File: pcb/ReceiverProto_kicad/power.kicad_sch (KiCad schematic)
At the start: 8 parts, among them U11 ADM8660ARZ-REEL, U12 ADP7182AUJZ-1.8-R7

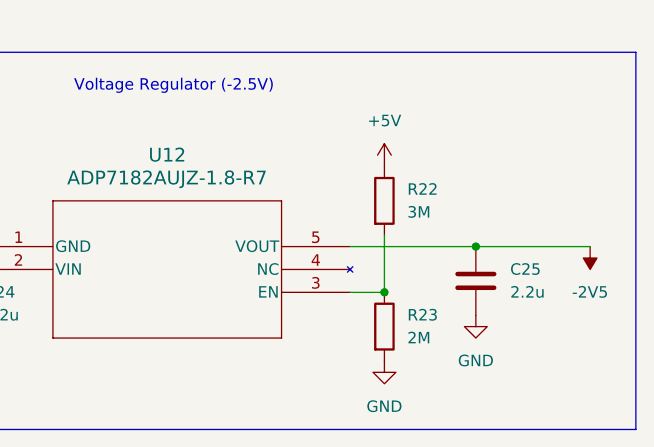
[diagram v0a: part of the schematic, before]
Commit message: added I/O for ADC interface, other slight tweaks
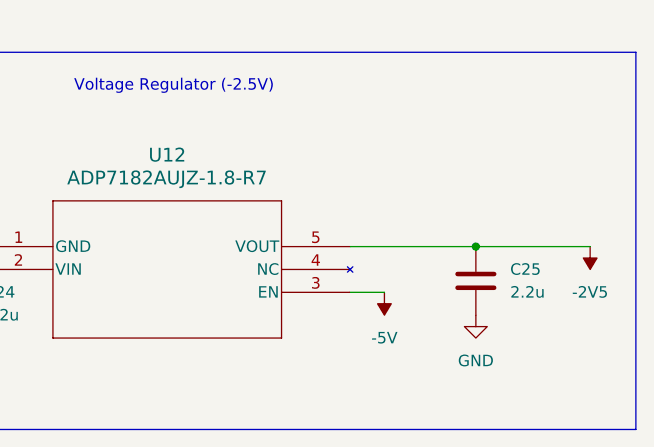
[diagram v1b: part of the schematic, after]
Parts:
- removed R22: 3M, symbol Device:R
- removed R23: 2M, symbol Device:R
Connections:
- net -5V: now also U12.3 (EN)
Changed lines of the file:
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@@
 		(color 0 0 0 0)
 	)
-	(junction
-		(at 234.95 72.39)
-		(diameter 0)
-		(color 0 0 0 0)
-	)
 	(wire
 		(pts
@@
 		(pts
 			(xy 231.14 72.39) (xy 234.95 72.39)
-		)
-		(stroke
-			(width 0)
-			(type default)
-		)
-	)
-	(wire
-		(pts
-			(xy 234.95 66.04) (xy 234.95 72.39)
 		)
 		(stroke
@@
 	)
 	(symbol
-		(lib_id "Device:R")
-		(at 234.95 62.23 0)
-		(unit 1)
-		(exclude_from_sim no)
-		(in_bom yes)
-		(on_board yes)
-		(dnp no)
-		(fields_autoplaced yes)
-		(property "Reference" "R22"
-			(at 237.49 60.9599 0)
-			(effects
-				(font
-					(size 1.27 1.27)
-				)
-				(justify left)
-			)
-		)
-		(property "Value" "3M"
-			(at 237.49 63.4999 0)
-			(effects
-				(font
-					(size 1.27 1.27)
-				)
-				(justify left)
-			)
-		)
-		(property "Footprint" ""
-			(at 233.172 62.23 90)
-			(effects
-				(font
-					(size 1.27 1.27)
-				)
-				(hide yes)
-			)
-		)
-		(property "Datasheet" "~"
-			(at 234.95 62.23 0)
-			(effects
-				(font
-					(size 1.27 1.27)
-				)
-				(hide yes)
-			)
-		)
-		(property "Description" "Resistor"
-			(at 234.95 62.23 0)
-			(effects
-				(font
-					(size 1.27 1.27)
-				)
-				(hide yes)
-			)
-		)
-		(pin "1"
-		)
-		(pin "2"
-		)
-		(instances
-			(project ""
-				(path "/1f346c8c-1e51-4f75-85ee-2d30c45e3fc5/93d8b42a-fb95-4bca-8da9-6ca00464e9a7"
-					(reference "R22")
-					(unit 1)
-				)
-			)
-		)
-	)
-	(symbol
 		(lib_id "power:-2V5")
 		(at 257.81 67.31 180)
@@
 	)
 	(symbol
-		(lib_id "Device:R")
-		(at 234.95 76.2 0)
-		(unit 1)
-		(exclude_from_sim no)
-		(in_bom yes)
-		(on_board yes)
-		(dnp no)
-		(fields_autoplaced yes)
-		(property "Reference" "R23"
-			(at 237.49 74.9299 0)
-			(effects
-				(font
-					(size 1.27 1.27)
-				)
-				(justify left)
-			)
-		)
-		(property "Value" "2M"
-			(at 237.49 77.4699 0)
-			(effects
-				(font
-					(size 1.27 1.27)
-				)
-				(justify left)
-			)
-		)
-		(property "Footprint" ""
-			(at 233.172 76.2 90)
-			(effects
-				(font
-					(size 1.27 1.27)
-				)
-				(hide yes)
-			)
-		)
-		(property "Datasheet" "~"
-			(at 234.95 76.2 0)
-			(effects
-				(font
-					(size 1.27 1.27)
-				)
-				(hide yes)
-			)
-		)
-		(property "Description" "Resistor"
-			(at 234.95 76.2 0)
-			(effects
-				(font
-					(size 1.27 1.27)
-				)
-				(hide yes)
-			)
-		)
-		(pin "1"
-		)
-		(pin "2"
-		)
-		(instances
-			(project ""
-				(path "/1f346c8c-1e51-4f75-85ee-2d30c45e3fc5/93d8b42a-fb95-4bca-8da9-6ca00464e9a7"
-					(reference "R23")
-					(unit 1)
-				)
-			)
-		)
-	)
-	(symbol
 		(lib_id "power:GND")
 		(at 186.69 77.47 0)
@@
 	)
 	(symbol
-		(lib_id "power:+5V")
-		(at 234.95 58.42 0)
-		(unit 1)
-		(exclude_from_sim no)
-		(in_bom yes)
-		(on_board yes)
-		(dnp no)
-		(fields_autoplaced yes)
-		(property "Reference" "#PWR057"
-			(at 234.95 62.23 0)
-			(effects
-				(font
-					(size 1.27 1.27)
-				)
-				(hide yes)
-			)
-		)
-		(property "Value" "+5V"
-			(at 234.95 53.34 0)
-			(effects
-				(font
-					(size 1.27 1.27)
-				)
-			)
-		)
-		(property "Footprint" ""
-			(at 234.95 58.42 0)
-			(effects
-				(font
-					(size 1.27 1.27)
-				)
-				(hide yes)
-			)
-		)
-		(property "Datasheet" ""
-			(at 234.95 58.42 0)
-			(effects
-				(font
-					(size 1.27 1.27)
-				)
-				(hide yes)
-			)
-		)
-		(property "Description" "Power symbol creates a global label with name \"+5V\""
-			(at 234.95 58.42 0)
-			(effects
-				(font
-					(size 1.27 1.27)
-				)
-				(hide yes)
-			)
-		)
-		(pin "1"
-		)
-		(instances
-			(project ""
-				(path "/1f346c8c-1e51-4f75-85ee-2d30c45e3fc5/93d8b42a-fb95-4bca-8da9-6ca00464e9a7"
-					(reference "#PWR057")
-					(unit 1)
-				)
-			)
-		)
-	)
-	(symbol
 		(lib_id "Device:C")
 		(at 186.69 73.66 0)
@@
 	)
 	(symbol
+		(lib_id "power:-5V")
+		(at 234.95 72.39 180)
+		(unit 1)
+		(exclude_from_sim no)
+		(in_bom yes)
+		(on_board yes)
+		(dnp no)
+		(fields_autoplaced yes)
+		(property "Reference" "#PWR046"
+			(at 234.95 74.93 0)
+			(effects
+				(font
+					(size 1.27 1.27)
+				)
+				(hide yes)
+			)
+		)
+		(property "Value" "-5V"
+			(at 234.95 77.47 0)
+			(effects
+				(font
+					(size 1.27 1.27)
+				)
+			)
+		)
+		(property "Footprint" ""
+			(at 234.95 72.39 0)
+			(effects
+				(font
+					(size 1.27 1.27)
+				)
+				(hide yes)
+			)
+		)
+		(property "Datasheet" ""
+			(at 234.95 72.39 0)
+			(effects
+				(font
+					(size 1.27 1.27)
+				)
+				(hide yes)
+			)
+		)
+		(property "Description" "Power symbol creates a global label with name \"-5V\""
+			(at 234.95 72.39 0)
+			(effects
+				(font
+					(size 1.27 1.27)
+				)
+				(hide yes)
+			)
+		)
+		(pin "1"
+		)
+		(instances
+			(project ""
+				(path "/1f346c8c-1e51-4f75-85ee-2d30c45e3fc5/93d8b42a-fb95-4bca-8da9-6ca00464e9a7"
+					(reference "#PWR046")
+					(unit 1)
+				)
+			)
+		)
+	)
+	(symbol
 		(lib_id "LDO_Regulator:ADP7182AUJZ-1.8-R7")
 		(at 190.5 67.31 0)
@@
 					(unit 1)
 				)
-			)
-		)
-	)
-	(symbol
-		(lib_id "power:GND")
-		(at 234.95 80.01 0)
-		(unit 1)
-		(exclude_from_sim no)
-		(in_bom yes)
-		(on_board yes)
-		(dnp no)
-		(fields_autoplaced yes)
-		(property "Reference" "#PWR056"
-			(at 234.95 86.36 0)
-			(effects
-				(font
-					(size 1.27 1.27)
-				)
-				(hide yes)
-			)
-		)
-		(property "Value" "GND"
-			(at 234.95 85.09 0)
-			(effects
-				(font
-					(size 1.27 1.27)
-				)
-			)
-		)
-		(property "Footprint" ""
-			(at 234.95 80.01 0)
-			(effects
-				(font
-					(size 1.27 1.27)
-				)
-				(hide yes)
-			)
-		)
-		(property "Datasheet" ""
-			(at 234.95 80.01 0)
-			(effects
-				(font
-					(size 1.27 1.27)
-				)
-				(hide yes)
-			)
-		)
-		(property "Description" "Power symbol creates a global label with name \"GND\" , ground"
-			(at 234.95 80.01 0)
-			(effects
-				(font
-					(size 1.27 1.27)
-				)
-				(hide yes)
-			)
-		)
-		(pin "1"
-		)
-		(instances
-			(project ""
-				(path "/1f346c8c-1e51-4f75-85ee-2d30c45e3fc5/93d8b42a-fb95-4bca-8da9-6ca00464e9a7"
-					(reference "#PWR056")
-					(unit 1)
-				)

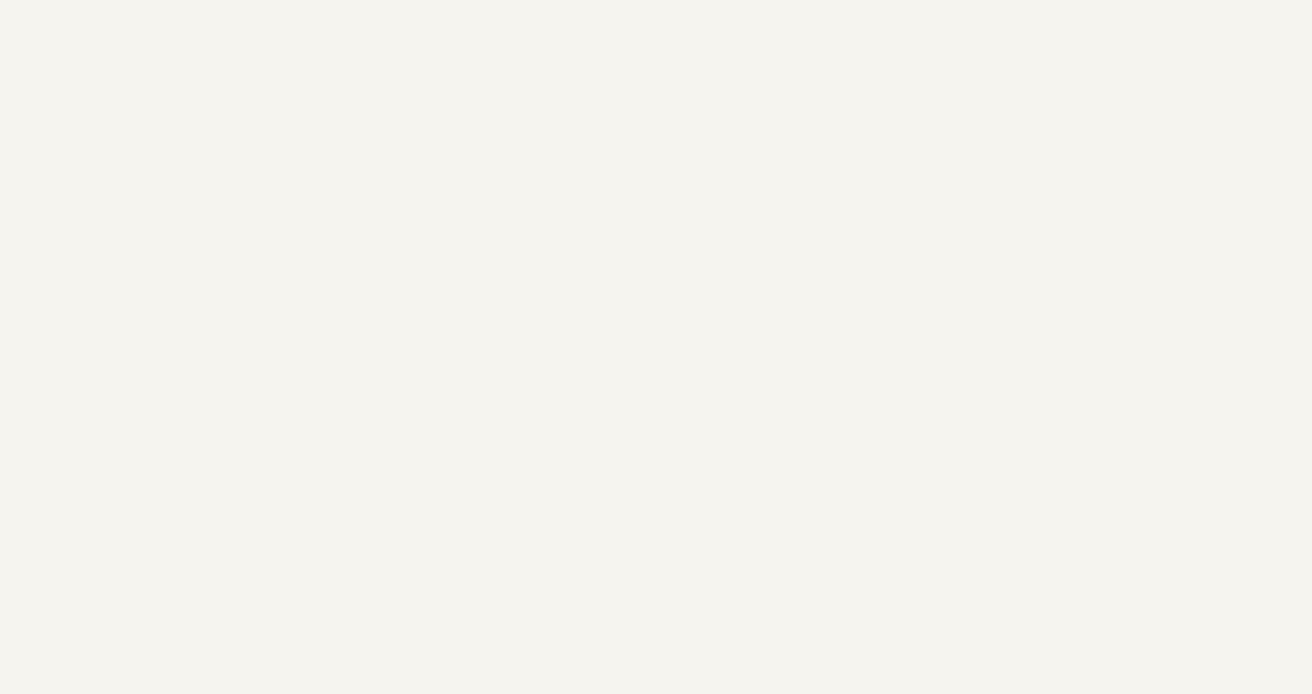
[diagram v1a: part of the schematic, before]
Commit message: created 3.3V voltage regulator circuit, as well implemented the amplifier in the frontend.
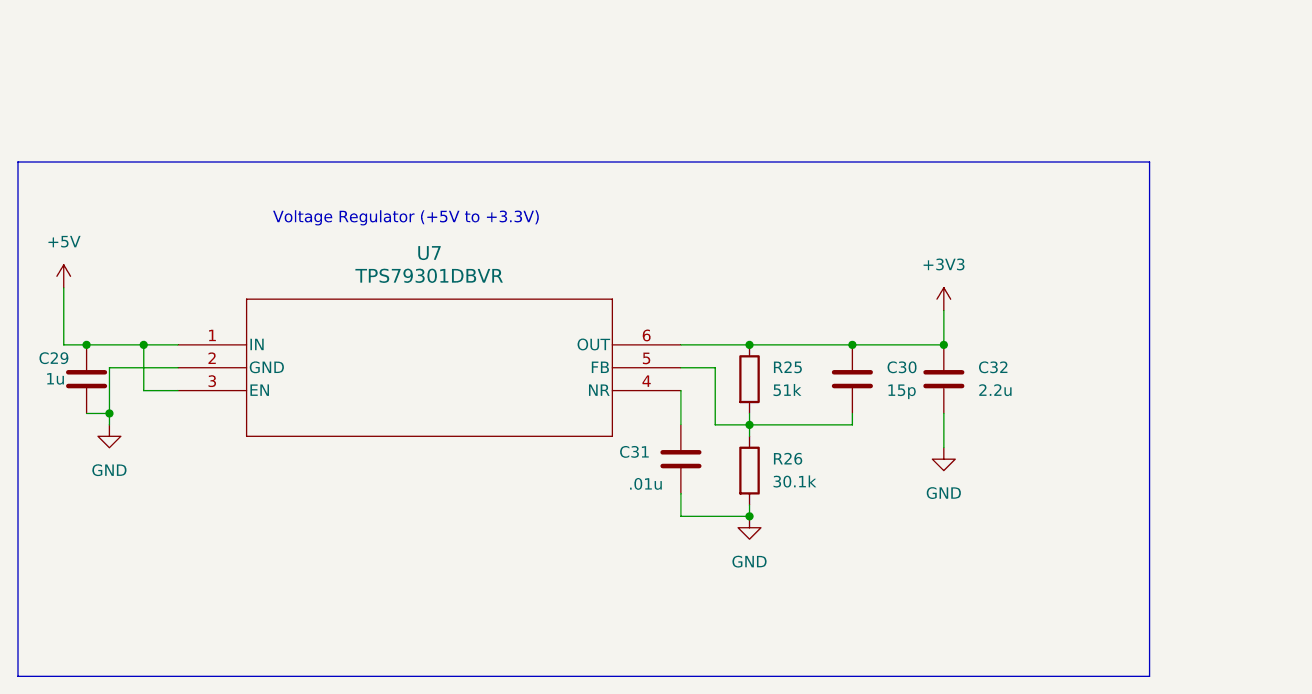
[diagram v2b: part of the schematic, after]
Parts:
- added C29: 1u, symbol Device:C
- added C30: 15p, symbol Device:C
- added C31: .01u, symbol Device:C
- added C32: 2.2u, symbol Device:C
- added R25: 51k, symbol Device:R
- added R26: 30.1k, symbol Device:R
- added U7: TPS79301DBVR, DBV6, symbol LDO_Regulator:TPS79301DBVR
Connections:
- net +5V: now also C29.1, U7.1 (IN), U7.3 (EN)
- net GND: now also C29.2, C31.2, C32.2, R26.2, U7.2 (GND)
- new net: C31.1, U7.4 (NR)
- new net: C30.2, R25.2, R26.1, U7.5 (FB)
- new net +3V3: C30.1, C32.1, R25.1, U7.6 (OUT)
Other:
- note added: "Voltage Regulator (+5V to +3.3V)"

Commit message: Modified voltage divider on ADC driver, and assigned footprints for all components in power schematic and ADC schematic.
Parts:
- C22, C23, C24, C25, C29, C30, C31, C32: footprint (none) -> Capacitor_SMD:C_0402_1005Metric
- R25, R26: footprint (none) -> Resistor_SMD:R_0201_0603Metric
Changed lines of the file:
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@@
 			)
 		)
-		(property "Footprint" ""
+		(property "Footprint" "Capacitor_SMD:C_0402_1005Metric"
 			(at 32.7152 147.32 0)
 			(effects
@@
 			)
 		)
-		(property "Footprint" ""
+		(property "Footprint" "Capacitor_SMD:C_0402_1005Metric"
 			(at 246.0752 74.93 0)
 			(effects
@@
 			)
 		)
-		(property "Footprint" ""
+		(property "Footprint" "Capacitor_SMD:C_0402_1005Metric"
 			(at 127.9652 147.32 0)
 			(effects
@@
 			)
 		)
-		(property "Footprint" ""
+		(property "Footprint" "Capacitor_SMD:C_0402_1005Metric"
 			(at 187.6552 77.47 0)
 			(effects
@@
 			)
 		)
-		(property "Footprint" ""
+		(property "Footprint" "Capacitor_SMD:C_0402_1005Metric"
 			(at 95.5548 69.85 0)
 			(effects
@@
 			)
 		)
-		(property "Footprint" ""
+		(property "Footprint" "Capacitor_SMD:C_0402_1005Metric"
 			(at 117.8052 147.32 0)
 			(effects
@@
 			)
 		)
-		(property "Footprint" ""
+		(property "Footprint" "Resistor_SMD:R_0201_0603Metric"
 			(at 103.632 153.67 90)
 			(effects
@@
 			)
 		)
-		(property "Footprint" ""
+		(property "Footprint" "Resistor_SMD:R_0201_0603Metric"
 			(at 103.632 143.51 90)
 			(effects
@@
 			)
 		)
-		(property "Footprint" ""
+		(property "Footprint" "Capacitor_SMD:C_0402_1005Metric"
 			(at 98.7552 156.21 0)
 			(effects
@@
 			)
 		)
-		(property "Footprint" ""
+		(property "Footprint" "Capacitor_SMD:C_0402_1005Metric"
 			(at 39.0652 71.12 0)
 			(effects

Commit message: add footprints for remaining symbols; 3.3V regulator still needs footprint
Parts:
- U11: footprint R_8_ADI -> Voltage_Converter:R_8_ADI
- U12: footprint UJ-5_ADI -> LDO_Regulator:UJ-5_ADI
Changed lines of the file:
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@@
 			)
 		)
-		(property "Footprint" "UJ-5_ADI"
+		(property "Footprint" "LDO_Regulator:UJ-5_ADI"
 			(at 190.5 67.31 0)
 			(effects
@@
 			)
 		)
-		(property "Footprint" "R_8_ADI"
+		(property "Footprint" "Voltage_Converter:R_8_ADI"
 			(at 55.88 62.23 0)
 			(effects

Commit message: Fixed footprint for voltage regulator.
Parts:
- U11: footprint Voltage_Converter:R_8_ADI -> R_8_ADI
- U12: footprint LDO_Regulator:UJ-5_ADI -> UJ-5_ADI
- U7: footprint DBV6 -> Voltage_Regulator:DBV5_TEX
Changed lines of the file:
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@@
 			)
 		)
-		(property "Footprint" "DBV6"
+		(property "Footprint" "Voltage_Regulator:DBV5_TEX"
 			(at 41.91 139.7 0)
 			(effects
@@
 			)
 		)
-		(property "Footprint" "LDO_Regulator:UJ-5_ADI"
+		(property "Footprint" "UJ-5_ADI"
 			(at 190.5 67.31 0)
 			(effects
@@
 			)
 		)
-		(property "Footprint" "Voltage_Converter:R_8_ADI"
+		(property "Footprint" "R_8_ADI"
 			(at 55.88 62.23 0)
 			(effects

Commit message: updated capacitor footprints.
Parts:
- C22, C23: footprint Capacitor_SMD:C_0402_1005Metric -> Capacitor_SMD:CP_Elec_4x5.8
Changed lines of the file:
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@@
 			)
 		)
-		(property "Footprint" "Capacitor_SMD:C_0402_1005Metric"
+		(property "Footprint" "Capacitor_SMD:CP_Elec_4x5.8"
 			(at 95.5548 69.85 0)
 			(effects
@@
 			)
 		)
-		(property "Footprint" "Capacitor_SMD:C_0402_1005Metric"
+		(property "Footprint" "Capacitor_SMD:CP_Elec_4x5.8"
 			(at 39.0652 71.12 0)
 			(effects

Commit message: fixed kicad project, all footprints linked and no errors on board
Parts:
- U11: footprint R_8_ADI -> Voltage_Converter:R_8_ADI
- U12: footprint UJ-5_ADI -> LDO_Regulator:UJ-5_ADI
- U7: footprint Voltage_Regulator:DBV5_TEX -> Voltage_Regulator:DBV6
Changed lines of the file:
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@@
 			)
 		)
-		(property "Footprint" "Voltage_Regulator:DBV5_TEX"
+		(property "Footprint" "Voltage_Regulator:DBV6"
 			(at 41.91 139.7 0)
 			(effects
@@
 			)
 		)
-		(property "Footprint" "UJ-5_ADI"
+		(property "Footprint" "LDO_Regulator:UJ-5_ADI"
 			(at 190.5 67.31 0)
 			(effects
@@
 			)
 		)
-		(property "Footprint" "R_8_ADI"
+		(property "Footprint" "Voltage_Converter:R_8_ADI"
 			(at 55.88 62.23 0)
 			(effects

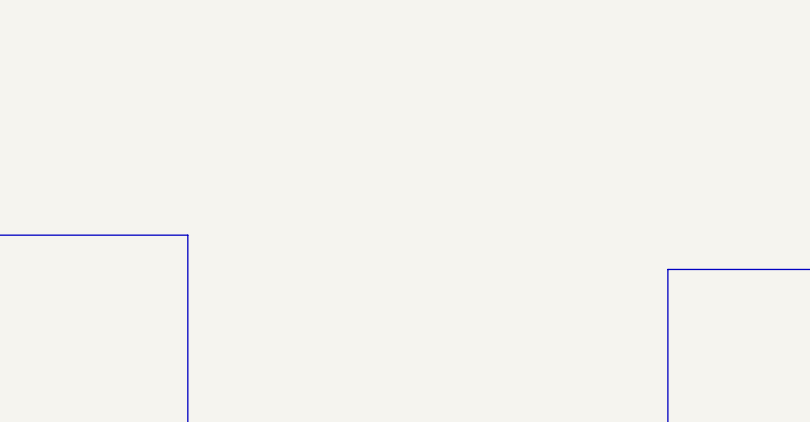
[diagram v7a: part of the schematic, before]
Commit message: add 5V filtering cap, reordered analog input pins
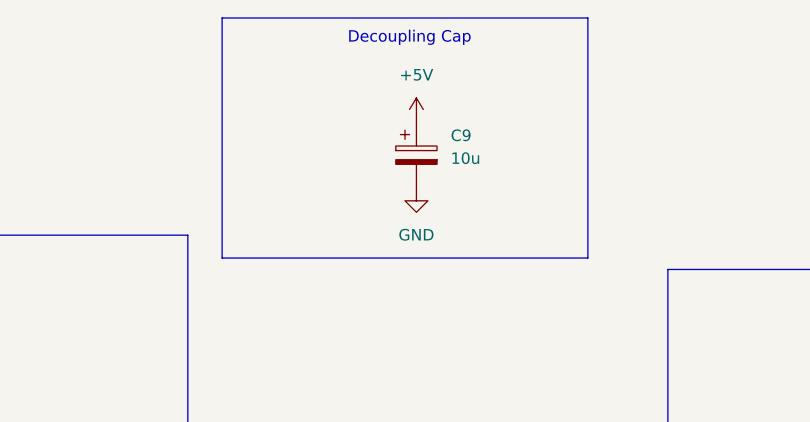
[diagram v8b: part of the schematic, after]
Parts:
- added C9: 10u, Capacitor_SMD:CP_Elec_4x5.8, symbol Device:C_Polarized
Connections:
- net +5V: now also C9.1
- net GND: now also C9.2
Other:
- note added: "Decoupling Cap"
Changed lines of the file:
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@@
+	)
+	(rectangle
+		(start 125.73 17.78)
+		(end 166.37 44.45)
+		(stroke
+			(width 0)
+			(type default)
+		)
+		(fill
+			(type none)
+		)
 	)
 	(rectangle
@@
 		(exclude_from_sim no)
 		(at 76.454 45.466 0)
+		(effects
+			(font
+				(size 1.27 1.27)
+			)
+		)
+	)
+	(text "Decoupling Cap"
+		(exclude_from_sim no)
+		(at 146.558 20.066 0)
 		(effects
 			(font
@@
 	)
 	(symbol
+		(lib_id "power:GND")
+		(at 147.32 36.83 0)
+		(unit 1)
+		(exclude_from_sim no)
+		(in_bom yes)
+		(on_board yes)
+		(dnp no)
+		(fields_autoplaced yes)
+		(property "Reference" "#PWR015"
+			(at 147.32 43.18 0)
+			(effects
+				(font
+					(size 1.27 1.27)
+				)
+				(hide yes)
+			)
+		)
+		(property "Value" "GND"
+			(at 147.32 41.91 0)
+			(effects
+				(font
+					(size 1.27 1.27)
+				)
+			)
+		)
+		(property "Footprint" ""
+			(at 147.32 36.83 0)
+			(effects
+				(font
+					(size 1.27 1.27)
+				)
+				(hide yes)
+			)
+		)
+		(property "Datasheet" ""
+			(at 147.32 36.83 0)
+			(effects
+				(font
+					(size 1.27 1.27)
+				)
+				(hide yes)
+			)
+		)
+		(property "Description" "Power symbol creates a global label with name \"GND\" , ground"
+			(at 147.32 36.83 0)
+			(effects
+				(font
+					(size 1.27 1.27)
+				)
+				(hide yes)
+			)
+		)
+		(pin "1"
+		)
+		(instances
+			(project ""
+				(path "/1f346c8c-1e51-4f75-85ee-2d30c45e3fc5/93d8b42a-fb95-4bca-8da9-6ca00464e9a7"
+					(reference "#PWR015")
+					(unit 1)
+				)
+			)
+		)
+	)
+	(symbol
 		(lib_id "Device:C")
 		(at 31.75 143.51 0)
@@
 	)
 	(symbol
+		(lib_id "Device:C_Polarized")
+		(at 147.32 33.02 0)
+		(unit 1)
+		(exclude_from_sim no)
+		(in_bom yes)
+		(on_board yes)
+		(dnp no)
+		(fields_autoplaced yes)
+		(property "Reference" "C9"
+			(at 151.13 30.8609 0)
+			(effects
+				(font
+					(size 1.27 1.27)
+				)
+				(justify left)
+			)
+		)
+		(property "Value" "10u"
+			(at 151.13 33.4009 0)
+			(effects
+				(font
+					(size 1.27 1.27)
+				)
+				(justify left)
+			)
+		)
+		(property "Footprint" "Capacitor_SMD:CP_Elec_4x5.8"
+			(at 148.2852 36.83 0)
+			(effects
+				(font
+					(size 1.27 1.27)
+				)
+				(hide yes)
+			)
+		)
+		(property "Datasheet" "~"
+			(at 147.32 33.02 0)
+			(effects
+				(font
+					(size 1.27 1.27)
+				)
+				(hide yes)
+			)
+		)
+		(property "Description" "Polarized capacitor"
+			(at 147.32 33.02 0)
+			(effects
+				(font
+					(size 1.27 1.27)
+				)
+				(hide yes)
+			)
+		)
+		(pin "1"
+		)
+		(pin "2"
+		)
+		(instances
+			(project ""
+				(path "/1f346c8c-1e51-4f75-85ee-2d30c45e3fc5/93d8b42a-fb95-4bca-8da9-6ca00464e9a7"
+					(reference "C9")
+					(unit 1)
+				)
+			)
+		)
+	)
+	(symbol
 		(lib_id "Device:R")
 		(at 105.41 143.51 0)
@@
 					(unit 1)
 				)
+			)
+		)
+	)
+	(symbol
+		(lib_id "power:+5V")
+		(at 147.32 29.21 0)
+		(unit 1)
+		(exclude_from_sim no)
+		(in_bom yes)
+		(on_board yes)
+		(dnp no)
+		(fields_autoplaced yes)
+		(property "Reference" "#PWR014"
+			(at 147.32 33.02 0)
+			(effects
+				(font
+					(size 1.27 1.27)
+				)
+				(hide yes)
+			)
+		)
+		(property "Value" "+5V"
+			(at 147.32 24.13 0)
+			(effects
+				(font
+					(size 1.27 1.27)
+				)
+			)
+		)
+		(property "Footprint" ""
+			(at 147.32 29.21 0)
+			(effects
+				(font
+					(size 1.27 1.27)
+				)
+				(hide yes)
+			)
+		)
+		(property "Datasheet" ""
+			(at 147.32 29.21 0)
+			(effects
+				(font
+					(size 1.27 1.27)
+				)
+				(hide yes)
+			)
+		)
+		(property "Description" "Power symbol creates a global label with name \"+5V\""
+			(at 147.32 29.21 0)
+			(effects
+				(font
+					(size 1.27 1.27)
+				)
+				(hide yes)
+			)
+		)
+		(pin "1"
+		)
+		(instances
+			(project ""
+				(path "/1f346c8c-1e51-4f75-85ee-2d30c45e3fc5/93d8b42a-fb95-4bca-8da9-6ca00464e9a7"
+					(reference "#PWR014")
+					(unit 1)
+				)
